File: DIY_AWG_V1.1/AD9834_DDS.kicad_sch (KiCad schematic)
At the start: 67 parts, among them IC1 TLV3544IPWR, IC2 ADG704BRMZ-REEL7, U11 8121H-50.000NK33DRL, U12 AD9834, U13 OPA2171AIDR

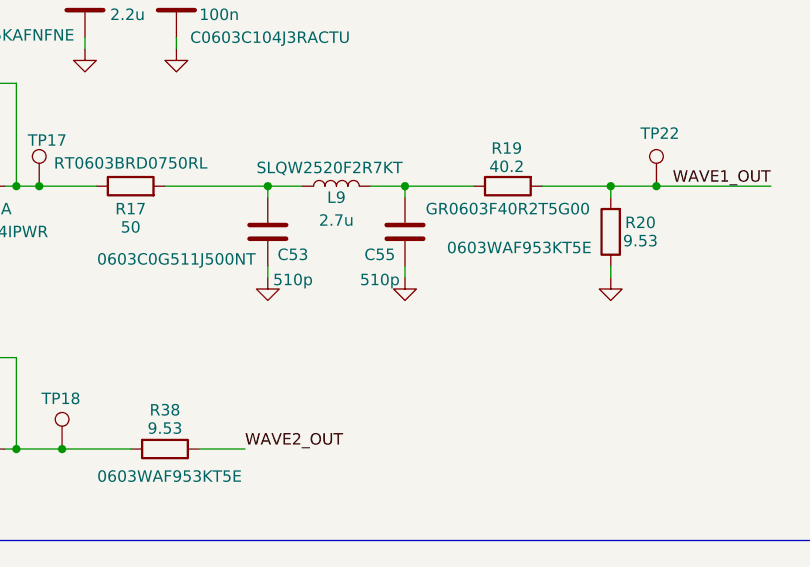
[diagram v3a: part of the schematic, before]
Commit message: Updated schematic footprints
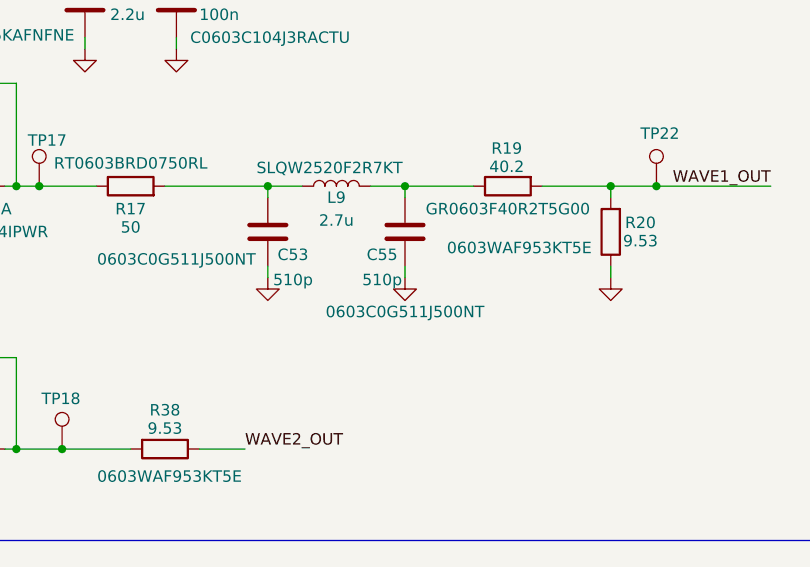
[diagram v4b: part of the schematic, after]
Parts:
- C55: footprint (none) -> Capacitor_SMD:C_0603_1608Metric; Component Name (none) -> 0603C0G511J500NT; LCSC ID (none) -> C49326333
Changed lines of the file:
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@@
 	)
 	(symbol
-		(lib_id "Device:C")
-		(at 102.87 101.6 0)
-		(mirror x)
-		(unit 1)
-		(body_style 1)
-		(exclude_from_sim no)
-		(in_bom yes)
-		(on_board yes)
-		(in_pos_files yes)
-		(dnp no)
-		(property "Reference" "C55"
-			(at 100.076 104.14 0)
-			(show_name no)
-			(do_not_autoplace no)
-			(effects
-				(font
-					(size 1.27 1.27)
-				)
-			)
-		)
-		(property "Value" "510p"
-			(at 100.076 106.934 0)
-			(show_name no)
-			(do_not_autoplace no)
-			(effects
-				(font
-					(size 1.27 1.27)
-				)
-			)
-		)
-		(property "Footprint" ""
-			(at 103.8352 97.79 0)
-			(hide yes)
-			(show_name no)
-			(do_not_autoplace no)
-			(effects
-				(font
-					(size 1.27 1.27)
-				)
-			)
-		)
-		(property "Datasheet" ""
-			(at 102.87 101.6 0)
-			(hide yes)
-			(show_name no)
-			(do_not_autoplace no)
-			(effects
-				(font
-					(size 1.27 1.27)
-				)
-			)
-		)
-		(property "Description" "Unpolarized capacitor"
-			(at 102.87 101.6 0)
-			(hide yes)
-			(show_name no)
-			(do_not_autoplace no)
-			(effects
-				(font
-					(size 1.27 1.27)
-				)
-			)
-		)
-		(pin "2"
-		)
-		(pin "1"
-		)
-		(instances
-			(project "DIY_AWG_V1.1"
-				(path "/508078af-d961-4af3-840e-a064a9f8d5bc/1a114e8b-a4a5-4450-90ed-0b55a984bade"
-					(reference "C55")
-					(unit 1)
-				)
-			)
-		)
-	)
-	(symbol
 		(lib_id "power:GND")
 		(at 34.29 50.8 0)
@@
 					(unit 1)
 				)
+			)
+		)
+	)
+	(symbol
+		(lib_id "Device:C")
+		(at 102.87 101.6 0)
+		(mirror x)
+		(unit 1)
+		(body_style 1)
+		(exclude_from_sim no)
+		(in_bom yes)
+		(on_board yes)
+		(in_pos_files yes)
+		(dnp no)
+		(property "Reference" "C55"
+			(at 100.33 104.14 0)
+			(show_name no)
+			(do_not_autoplace no)
+			(effects
+				(font
+					(size 1.27 1.27)
+				)
+			)
+		)
+		(property "Value" "510p"
+			(at 100.33 106.934 0)
+			(show_name no)
+			(do_not_autoplace no)
+			(effects
+				(font
+					(size 1.27 1.27)
+				)
+			)
+		)
+		(property "Footprint" "Capacitor_SMD:C_0603_1608Metric"
+			(at 103.8352 97.79 0)
+			(hide yes)
+			(show_name no)
+			(do_not_autoplace no)
+			(effects
+				(font
+					(size 1.27 1.27)
+				)
+			)
+		)
+		(property "Datasheet" "https://www.lcsc.com/datasheet/C49326333.pdf?spm=wm.sxq.inf.ggs___wm.fly.bg.24.xh&lcsc_vid=EVldUV1eRAJaUwYHFAdaVVJVQFRYUFFWFAdfXgVUElQxVlNeQlRXUVRSTlZaXzsOAxUeFF5JWBYZEEoKFBINSQcJGk4NBhADEA4cHktXRlVcSQwSGg0%3D"
+			(at 102.87 101.6 0)
+			(hide yes)
+			(show_name no)
+			(do_not_autoplace no)
+			(effects
+				(font
+					(size 1.27 1.27)
+				)
+			)
+		)
+		(property "Description" "Unpolarized capacitor"
+			(at 102.87 101.6 0)
+			(hide yes)
+			(show_name no)
+			(do_not_autoplace no)
+			(effects
+				(font
+					(size 1.27 1.27)
+				)
+			)
+		)
+		(property "Component Name" "0603C0G511J500NT"
+			(at 102.87 110.49 0)
+			(show_name no)
+			(do_not_autoplace no)
+			(effects
+				(font
+					(size 1.27 1.27)
+				)
+			)
+		)
+		(property "LCSC ID" "C49326333"
+			(at 102.87 101.6 0)
+			(hide yes)
+			(show_name no)
+			(do_not_autoplace no)
+			(effects
+				(font
+					(size 1.27 1.27)
+				)
+			)
+		)
+		(pin "2"
+		)
+		(pin "1"
+		)
+		(instances
+			(project "DIY_AWG_V1.1"
+				(path "/508078af-d961-4af3-840e-a064a9f8d5bc/1a114e8b-a4a5-4450-90ed-0b55a984bade"
+					(reference "C55")
+					(unit 1)
+				)

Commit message: Updated schematics
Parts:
- removed TP12, TP15, TP16, TP22, TP23, TP24, TP25, TP26: TestPoint, symbol Connector:TestPoint
- added Je1: Conn_01x04_Pin, Connector_PinHeader_2.54mm:PinHeader_1x04_P2.54mm_Vertical, symbol Connector:Conn_01x04_Pin
- added R14, R18, R22, R24: 0, Resistor_SMD:R_0603_1608Metric, symbol Device:R
- added RF6, RF7, RF8, RF9: IPEX-01, easyeda2kicad:IPEX-SMD_3P-L2.6-W2.6-LS3.0_YUANDI_RF-001, symbol easyeda2kicad:IPEX-01
- added TP19, TP20: TestPoint, TestPoint:TestPoint_Pad_D2.0mm, symbol Connector:TestPoint
- TP13, TP14, TP17, TP18, TP21: footprint (none) -> TestPoint:TestPoint_Pad_D2.0mm
- TP15: renamed from TP19; footprint (none) -> TestPoint:TestPoint_Pad_D2.0mm
- TP16: renamed from TP20; footprint (none) -> TestPoint:TestPoint_Pad_D2.0mm
- renumbered C62 to C45, C31 to C46, C45 to C47, C46 to C48, C47 to C49, C56 to C50, C53 to C51, C50 to C52, C59 to C53, C48 to C54, C58 to C55, C61 to C56, C55 to C57, C51 to C58, C63 to C59, C52 to C60, C64 to C61, C54 to C62, C57 to C63, C60 to C64, C88 to C65, L9 to L8, L8 to L9, R14 to R15, R15 to R16, R39 to R17, R17 to R19, R38 to R20, R19 to R21, R20 to R23, R24 to R25, R16 to R26, R22 to R27, R23 to R28, R21 to R29, R25 to R30, R27 to R31, R18 to R32, R26 to R33
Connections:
- net DC_GAIN: now also TP19.1
- net DC_OFFSET: now also TP20.1
- net GND: now also TP13.1, TP18.1, TP21.1, RF6.2, RF6.3, RF7.2, RF7.3, RF8.2, RF8.3, RF9.2, RF9.3
- net MUX1_OUT: now also R22.1; no longer TP21.1
- net REF_SIG1: now also TP17.1
- net SPI2_CS: now also Je1.3 (Pin_3)
- net SPI2_MOSI: now also Je1.2 (Pin_2); no longer TP14.1
- net SPI2_RESET: now also Je1.4 (Pin_4)
- net SPI2_SCLK: now also Je1.1 (Pin_1); no longer TP13.1
- net SQUARE_OUT: now also R14.1
- net WAVE1_OUT: now also R24.1
- net at U11.3 (OUT), U12.8 (MCLK): now also TP14.1
- net at IC1.6 (INB-), IC1.7 (OUTB), R20.2: now also R18.1; no longer TP18.1
- net at IC1.1 (OUTA), IC1.2 (INA-), R19.1: no longer TP17.1
- new net: R18.2, RF7.1
- new net: R22.2, RF8.1
- new net: R24.2, RF9.1
- new net: R14.2, RF6.1
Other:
- note added: "A: Custom Waveform from STM32 DAC B: Sine Waveform from AD9834 C: DC Gain for LMH6505 D: Grounded"
- note removed: "A: Custom Waveform from STM32 DAC B: Sine Waveform from AD9834 C: DC Gain for LMH6505 D: Constant 0.157V Reference"
- moved on the sheet: C45, C48, C50, C52, C53, C55, C56, C59, C61, IC1B, IC1C, IC1D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

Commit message: Updated PCB design, uploaded necessary footprints and symbols for some components
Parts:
- L8: footprint easyeda2kicad:L_SMD_SLQW2520_2.9x2.7 -> easyeda2kicad:L_1008_2520_SLQW2520
- TP13, TP14, TP15, TP16, TP17, TP18, TP19, TP20, TP21: footprint TestPoint:TestPoint_Pad_D2.0mm -> TestPoint:TestPoint_Pad_D1.0mm
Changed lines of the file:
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@@
 			)
 		)
-		(property "Footprint" "TestPoint:TestPoint_Pad_D2.0mm"
+		(property "Footprint" "TestPoint:TestPoint_Pad_D1.0mm"
 			(at 67.31 252.73 0)
 			(hide yes)
@@
 			)
 		)
-		(property "Footprint" "TestPoint:TestPoint_Pad_D2.0mm"
+		(property "Footprint" "TestPoint:TestPoint_Pad_D1.0mm"
 			(at 67.31 250.19 0)
 			(hide yes)
@@
 			)
 		)
-		(property "Footprint" "TestPoint:TestPoint_Pad_D2.0mm"
+		(property "Footprint" "TestPoint:TestPoint_Pad_D1.0mm"
 			(at 356.87 138.43 0)
 			(hide yes)
@@
 			)
 		)
-		(property "Footprint" "easyeda2kicad:L_SMD_SLQW2520_2.9x2.7"
+		(property "Footprint" "easyeda2kicad:L_1008_2520_SLQW2520"
 			(at 95.25 96.52 0)
 			(hide yes)
@@
 			)
 		)
-		(property "Footprint" "TestPoint:TestPoint_Pad_D2.0mm"
+		(property "Footprint" "TestPoint:TestPoint_Pad_D1.0mm"
 			(at 57.15 260.35 0)
 			(hide yes)
@@
 			)
 		)
-		(property "Footprint" "TestPoint:TestPoint_Pad_D2.0mm"
+		(property "Footprint" "TestPoint:TestPoint_Pad_D1.0mm"
 			(at 48.26 250.19 0)
 			(hide yes)
@@
 			)
 		)
-		(property "Footprint" "TestPoint:TestPoint_Pad_D2.0mm"
+		(property "Footprint" "TestPoint:TestPoint_Pad_D1.0mm"
 			(at 217.17 78.74 0)
 			(hide yes)
@@
 			)
 		)
-		(property "Footprint" "TestPoint:TestPoint_Pad_D2.0mm"
+		(property "Footprint" "TestPoint:TestPoint_Pad_D1.0mm"
 			(at 367.03 67.31 0)
 			(hide yes)
@@
 			)
 		)
-		(property "Footprint" "TestPoint:TestPoint_Pad_D2.0mm"
+		(property "Footprint" "TestPoint:TestPoint_Pad_D1.0mm"
 			(at 351.79 74.93 0)
 			(hide yes)
@@
 			)
 		)
-		(property "Footprint" "TestPoint:TestPoint_Pad_D2.0mm"
+		(property "Footprint" "TestPoint:TestPoint_Pad_D1.0mm"
 			(at 198.12 71.12 0)
 			(hide yes)

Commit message: Edited the electrical schematics, PCB design
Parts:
- removed RF6, RF7, RF8, RF9: IPEX-01, easyeda2kicad:IPEX-SMD_3P-L2.6-W2.6-LS3.0_YUANDI_RF-001, symbol easyeda2kicad:IPEX-01
- added CN6, CN7, CN8, CN9: RH-5019, easyeda2kicad:TESTPOINT-SMD_L3.8-W2.0_RH-5019, symbol easyeda2kicad:RH-5019
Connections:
- net at R18.2: now also CN7.1
- net at R22.2: now also CN9.1
- net at R24.2: now also CN6.1
- net at R14.2: now also CN8.1

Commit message: Updated schematic PCB design
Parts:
- added CN11, CN12: RH-5019, easyeda2kicad:TESTPOINT-SMD_L3.8-W2.0_RH-5019, symbol easyeda2kicad:RH-5019
- renumbered CN8 to CN6, CN9 to CN8, CN6 to CN9, R14 to R23, R15 to R24, R16 to R25, R17 to R26, R18 to R27, R19 to R28, R20 to R29, R21 to R30, R22 to R31, R23 to R32, R24 to R33, R25 to R34, R26 to R35, R27 to R36, R28 to R37, R29 to R38, R30 to R39, R31 to R40, R32 to R41, R33 to R42, TP13 to TP19, TP14 to TP20, TP15 to TP21, TP16 to TP22, TP17 to TP23, TP18 to TP24, TP19 to TP25, TP20 to TP26, TP21 to TP27
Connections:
- net FSELECT: now also CN12.1
- net GND: now also IC1.10 (INC+); no longer IC1.12 (IND+)
- net PSELECT: now also CN11.1
- net REF_SIG1: now also IC1.13 (IND-), IC1.14 (OUTD); no longer IC1.8 (OUTC), IC1.9 (INC-)
- net at R36.1, R37.1: now also IC1.12 (IND+); no longer IC1.10 (INC+)
- new net: IC1.8 (OUTC), IC1.9 (INC-)
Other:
- moved on the sheet: IC1C, IC1D, TP19
